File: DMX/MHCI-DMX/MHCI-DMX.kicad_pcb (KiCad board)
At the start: 2 copper layers, 79 x 90 mm, 73 parts, among them J1 XLR_Male, J10 Conn_01x02, J11 Conn_01x02, J12 Conn_01x02, J13 Conn_01x02, J14 Conn_01x02, J15 Conn_01x02, J16 Conn_01x04, J17 Conn_01x08, J18 Conn_01x04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

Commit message: v1.0 Production Files
Small ground connection fixed.
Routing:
- net GND: track 4.38 -> 6.13 mm
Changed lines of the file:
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@@
 				(font
 					(size 1.27 1.27)
+					(thickness 0.15)
 				)
 			)
@@
 				(font
 					(size 1.27 1.27)
+					(thickness 0.15)
 				)
 			)
@@
 				(font
 					(size 1.27 1.27)
+					(thickness 0.15)
 				)
 			)
@@
 				(font
 					(size 1.27 1.27)
+					(thickness 0.15)
 				)
 			)
@@
 				(font
 					(size 1.27 1.27)
+					(thickness 0.15)
 				)
 			)
@@
 				(font
 					(size 1.27 1.27)
+					(thickness 0.15)
 				)
 			)
@@
 				(font
 					(size 1.27 1.27)
+					(thickness 0.15)
 				)
 			)
@@
 				(font
 					(size 1.27 1.27)
+					(thickness 0.15)
 				)
 			)
@@
 				(font
 					(size 1.27 1.27)
+					(thickness 0.15)
 				)
 			)
@@
 				(font
 					(size 1.27 1.27)
+					(thickness 0.15)
 				)
 			)
@@
 				(font
 					(size 1.27 1.27)
+					(thickness 0.15)
 				)
 			)
@@
 				(font
 					(size 1.27 1.27)
+					(thickness 0.15)
 				)
 			)
@@
 				(font
 					(size 1.27 1.27)
+					(thickness 0.15)
 				)
 			)
@@
 				(font
 					(size 1.27 1.27)
+					(thickness 0.15)
 				)
 			)
@@
 				(font
 					(size 1.27 1.27)
+					(thickness 0.15)
 				)
 			)
@@
 				(font
 					(size 1.27 1.27)
+					(thickness 0.15)
 				)
 			)
@@
 				(font
 					(size 1.27 1.27)
+					(thickness 0.15)
 				)
 			)
@@
 				(font
 					(size 1.27 1.27)
+					(thickness 0.15)
 				)
 			)
@@
 				(font
 					(size 1.27 1.27)
+					(thickness 0.15)
 				)
 			)
@@
 				(font
 					(size 1.27 1.27)
+					(thickness 0.15)
 				)
 			)
@@
 				(font
 					(size 1.27 1.27)
+					(thickness 0.15)
 				)
 			)
@@
 				(font
 					(size 1.27 1.27)
+					(thickness 0.15)
 				)
 			)
@@
 				(font
 					(size 1.27 1.27)
+					(thickness 0.15)
 				)
 			)
@@
 				(font
 					(size 1.27 1.27)
+					(thickness 0.15)
 				)
 			)
@@
 				(font
 					(size 1.27 1.27)
+					(thickness 0.15)
 				)
 			)
@@
 				(font
 					(size 1.27 1.27)
+					(thickness 0.15)
 				)
 			)
@@
 				(font
 					(size 1.27 1.27)
+					(thickness 0.15)
 				)
 			)
@@
 				(font
 					(size 1.27 1.27)
+					(thickness 0.15)
 				)
 			)
@@
 				(font
 					(size 1.27 1.27)
+					(thickness 0.15)
 				)
 			)
@@
 				(font
 					(size 1.27 1.27)
+					(thickness 0.15)
 				)
 			)
@@
 				(font
 					(size 1.27 1.27)
+					(thickness 0.15)
 				)
 			)
@@
 				(font
 					(size 1.27 1.27)
+					(thickness 0.15)
 				)
 			)
@@
 				(font
 					(size 1.27 1.27)
+					(thickness 0.15)
 				)
 			)
@@
 				(font
 					(size 1.27 1.27)
+					(thickness 0.15)
 				)
 			)
@@
 				(font
 					(size 1.27 1.27)
+					(thickness 0.15)
 				)
 			)
@@
 				(font
 					(size 1.27 1.27)
+					(thickness 0.15)
 				)
 			)
@@
 				(font
 					(size 1.27 1.27)
+					(thickness 0.15)
 				)
 			)
@@
 				(font
 					(size 1.27 1.27)
+					(thickness 0.15)
 				)
 			)
@@
 				(font
 					(size 1.27 1.27)
+					(thickness 0.15)
 				)
 			)
@@
 	)
 	(segment
+		(start 115.895 96.125)
+		(end 115.895 95.815001)
+		(width 0.3)
+		(layer "F.Cu")
+		(net 2)
+	)
+	(segment
 		(start 76.3625 84.05)
 		(end 75.75 84.05)
@@
 		(layer "F.Cu")
 		(net 2)
+	)
+	(segment
+		(start 115.895 95.815001)
+		(end 116.710001 95)
+		(width 0.3)
+		(layer "F.Cu")
+		(net 2)
+	)
+	(segment
+		(start 116.710001 95)
+		(end 117 95)
+		(width 0.3)
+		(layer "F.Cu")
+		(net 2)

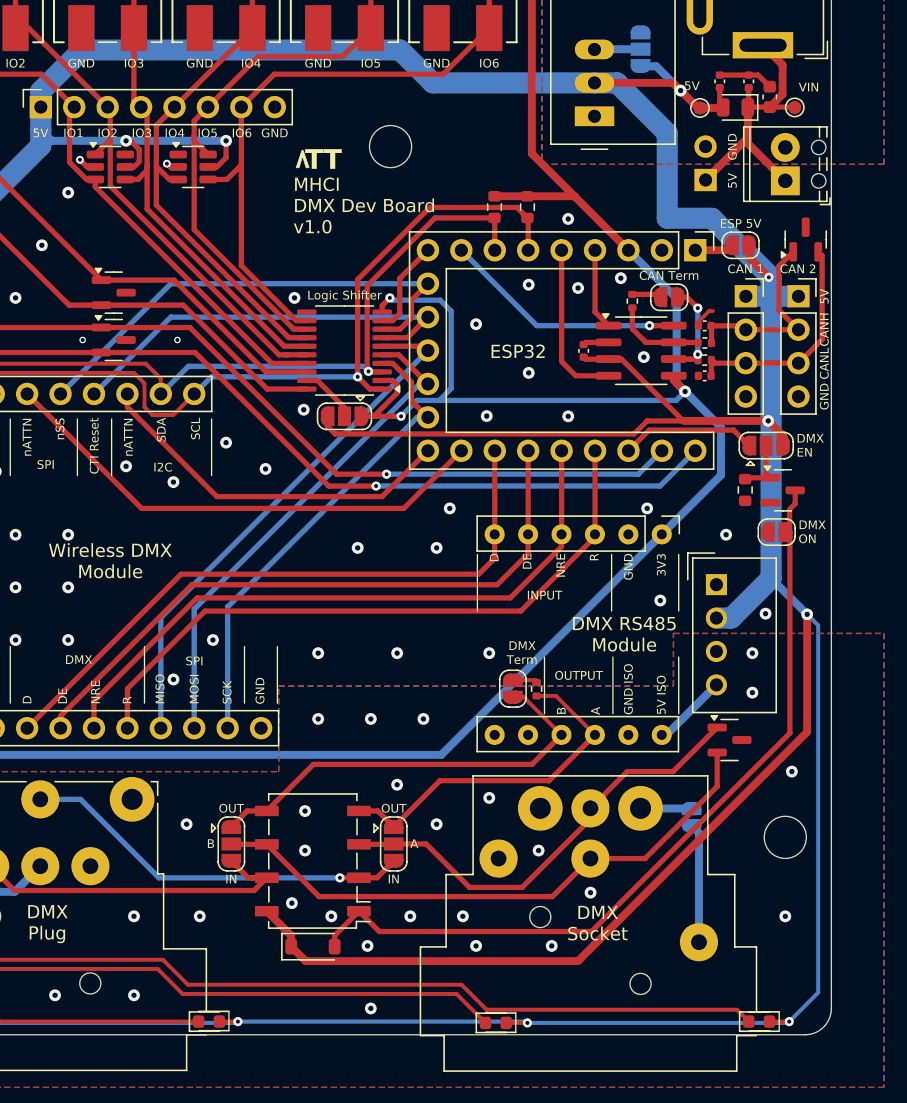
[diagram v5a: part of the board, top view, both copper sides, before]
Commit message: Update DMX board with v1.1 updates
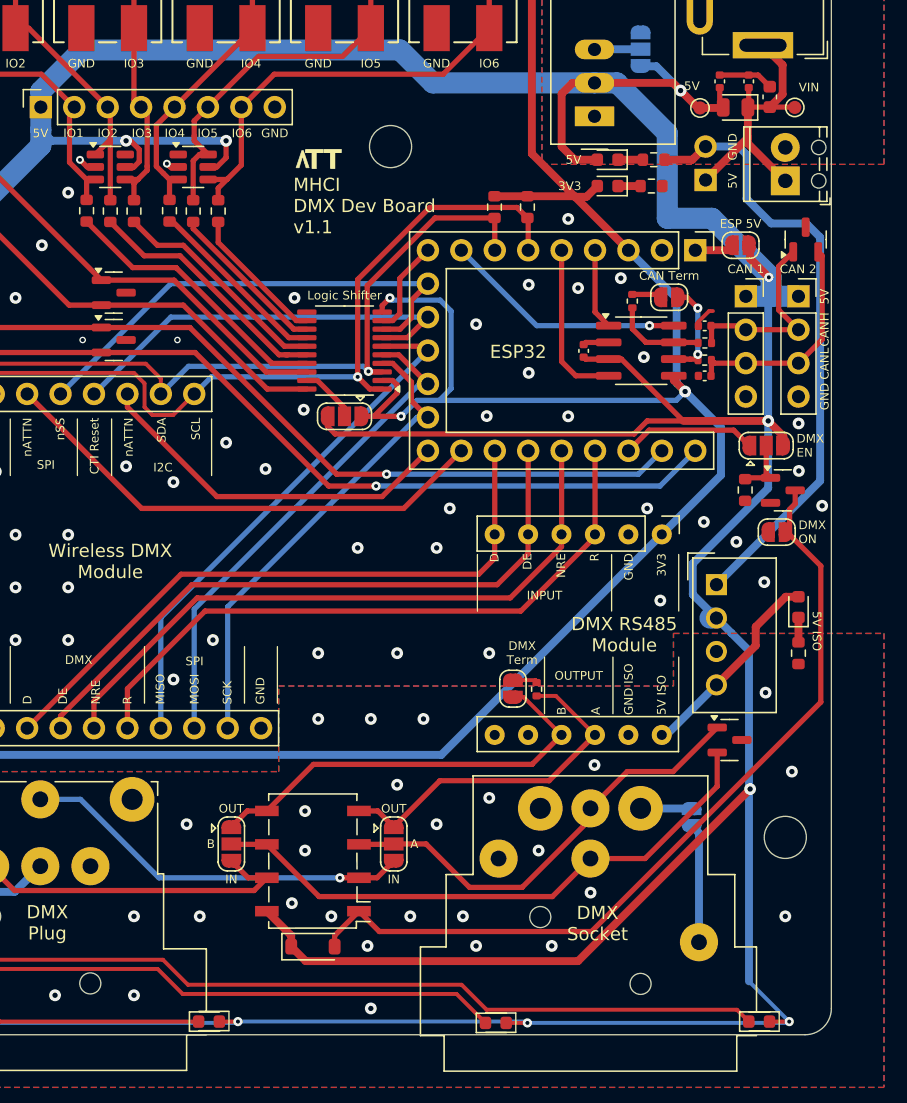
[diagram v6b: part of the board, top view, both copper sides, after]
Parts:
- added D11: RED, LED_SMD:LED_0603_1608Metric, F.Cu at (109.0, 83.5)
- added D12: RED, LED_SMD:LED_0603_1608Metric, F.Cu at (123.5, 117.5)
- added D13: RED, LED_SMD:LED_0603_1608Metric, F.Cu at (109.0, 85.5)
- added R14: 680R, Resistor_SMD:R_0603_1608Metric, F.Cu at (112.5, 83.5)
- added R15: 680R, Resistor_SMD:R_0603_1608Metric, F.Cu at (123.5, 121.0)
- added R16: 680R, Resistor_SMD:R_0603_1608Metric, F.Cu at (112.3, 85.5)
- added R17: 1K, Resistor_SMD:R_0603_1608Metric, F.Cu at (69.4, 87.4)
- added R18: 1K, Resistor_SMD:R_0603_1608Metric, F.Cu at (71.2, 87.4)
- added R19: 1K, Resistor_SMD:R_0603_1608Metric, F.Cu at (73.0, 87.4)
- added R20: 1K, Resistor_SMD:R_0603_1608Metric, F.Cu at (75.7, 87.4)
- added R21: 1K, Resistor_SMD:R_0603_1608Metric, F.Cu at (77.5, 87.4)
- added R22: 1K, Resistor_SMD:R_0603_1608Metric, F.Cu at (79.4, 87.4)
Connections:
- U5 pad 1: GND -> Earth
- U8 pad 12: GPIO_X6_5 -> Net-(U8-B8)
- U8 pad 13: GPIO_X5_5 -> Net-(U8-B7)
- U8 pad 14: GPIO_X4_5 -> Net-(U8-B6)
- U8 pad 15: GPIO_X3_5 -> Net-(U8-B5)
- U8 pad 16: GPIO_X2_5 -> Net-(U8-B4)
- U8 pad 17: GPIO_X1_5 -> Net-(U8-B3)
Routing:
- net Earth: track 4.17 -> 50.9 mm
- net Net-(U8-B3): track 0.00 -> 21.2 mm
- net GPIO_X1_5: track 54.2 -> 33.6 mm
- net GPIO_X2_5: track 46.9 -> 27.5 mm
- net Net-(U8-B4): track 0.00 -> 19.3 mm
- net GPIO_X3_5: track 41.8 -> 23.8 mm
- net Net-(U8-B5): track 0.00 -> 17.1 mm
- net GPIO_X4_5: track 43.4 -> 26.4 mm
- net GPIO_X5_5: track 47.4 -> 32.9 mm
- net Net-(U8-B6): track 0.00 -> 14.1 mm
- net GPIO_X6_5: track 52.3 -> 39.8 mm
- net Net-(U8-B7): track 0.00 -> 12.3 mm
- net Net-(U8-B8): track 0.00 -> 10.8 mm
- net +5V_ISO: track 5.73 -> 16.0 mm
- net +5V: track 371.5 -> 364.6 mm
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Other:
- board text added: "MHCI DMX Dev Board v1.1"
- board text removed: "MHCI DMX Dev Board v1.0"

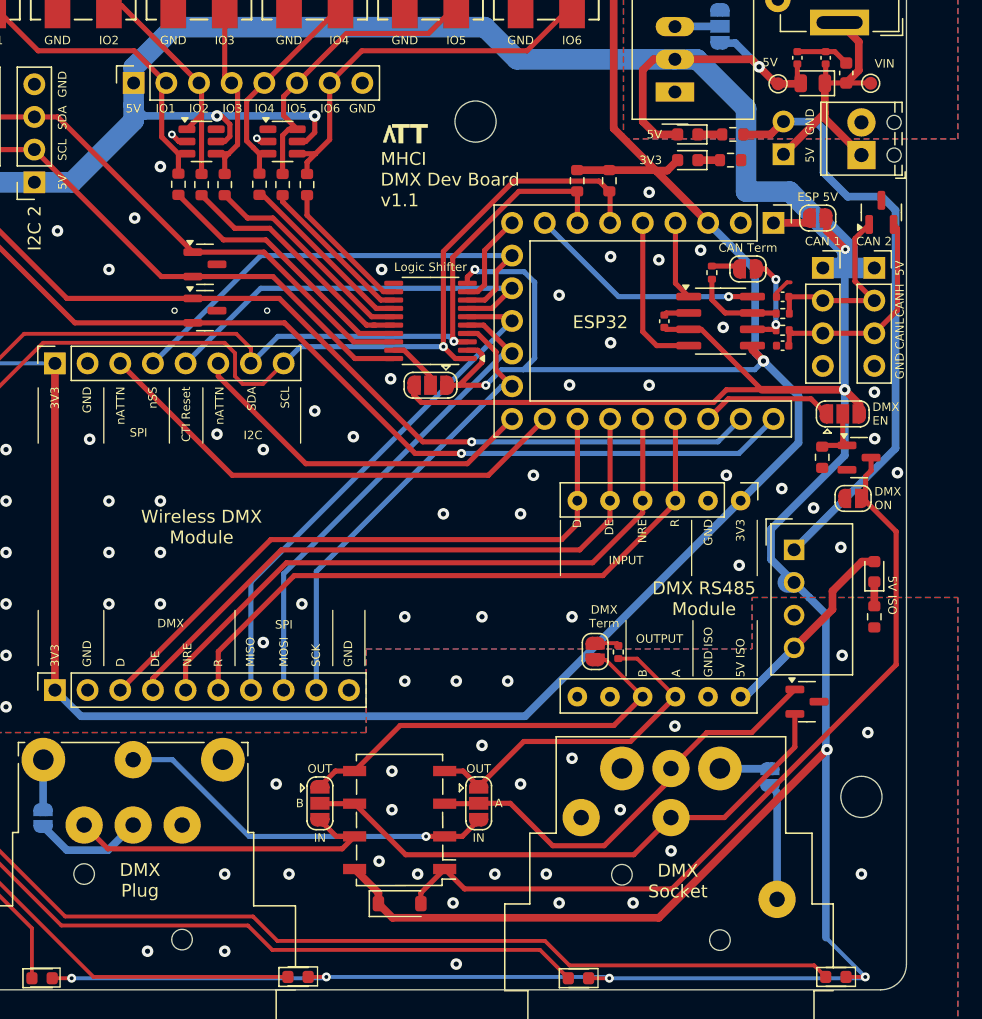
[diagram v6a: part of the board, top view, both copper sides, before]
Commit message: MHCI-DMX v1.1 hardware
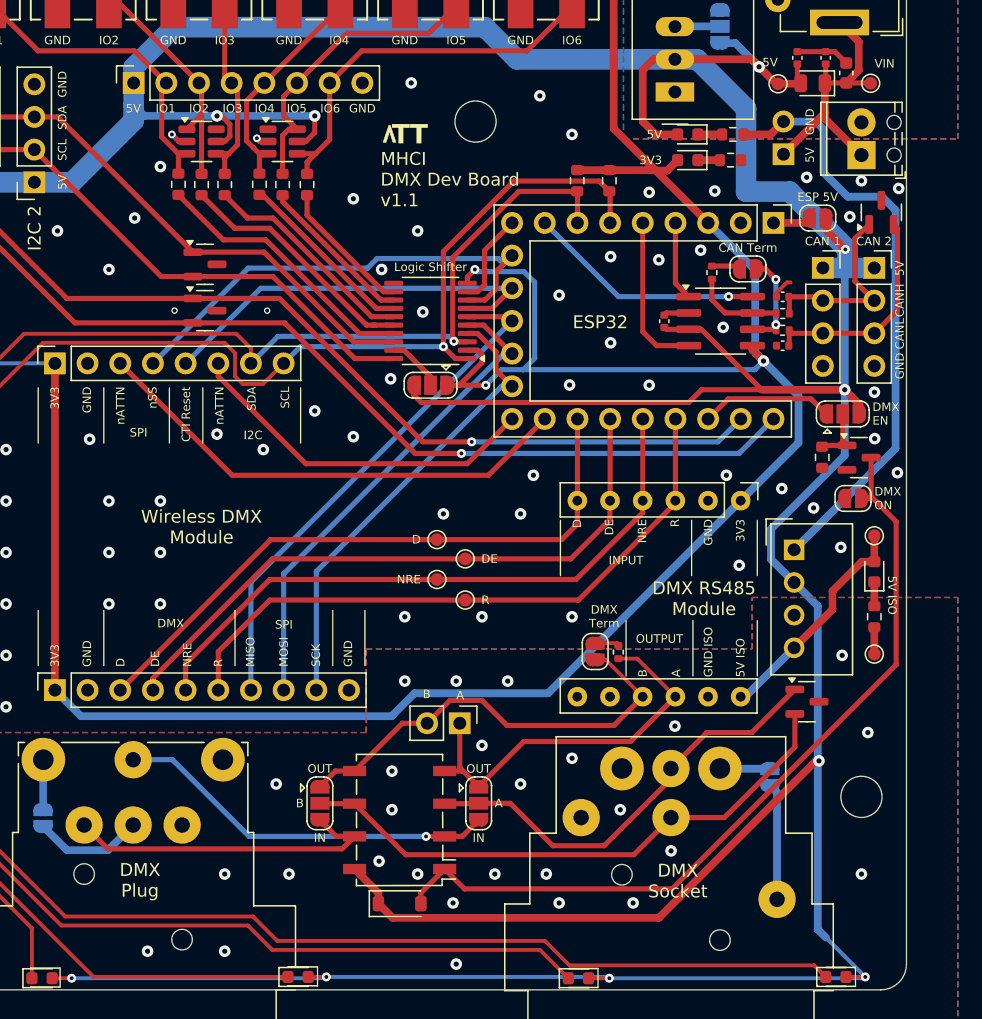
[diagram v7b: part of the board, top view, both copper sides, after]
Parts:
- added J19: Conn_01x02, Connector_PinHeader_2.54mm:PinHeader_1x02_P2.54mm_Vertical, F.Cu at (91.3, 129.3)
- added TP3: 5V_ISO, TestPoint:TestPoint_Pad_D1.0mm, F.Cu at (123.5, 114.7)
- added TP4: GND_DMX, TestPoint:TestPoint_Pad_D1.0mm, F.Cu at (123.5, 123.9)
- added TP5: D, TestPoint:TestPoint_Pad_D1.0mm, F.Cu at (89.5, 115.0)
- added TP6: DE, TestPoint:TestPoint_Pad_D1.0mm, F.Cu at (91.7, 116.5)
- added TP7: NRE, TestPoint:TestPoint_Pad_D1.0mm, F.Cu at (89.5, 118.1)
- added TP8: R, TestPoint:TestPoint_Pad_D1.0mm, F.Cu at (91.7, 119.7)
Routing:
- net A: track 26.9 -> 30.7 mm
- net GND_DMX: track 7.78 -> 9.86 mm
- net +5V_ISO: track 16.0 -> 18.1 mm
- net B: track 32.9 -> 34.5 mm
- net +5V: track 364.6 -> 363.1 mm
- net GND: vias 68 -> 77

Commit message: MHCI DMX v1.2 production files
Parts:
- removed J9: Conn_01x02, Connector_PinHeader_2.54mm:PinHeader_1x02_P2.54mm_Vertical
- removed TP1: VIN, TestPoint:TestPoint_Pad_D1.0mm
- removed TP2: 5V, TestPoint:TestPoint_Pad_D1.0mm
- added J3: Conn_01x02, Connector_PinHeader_2.54mm:PinHeader_1x02_P2.54mm_Vertical, F.Cu at (112.7, 73.1)
- added U6: TSR_2-2450, Converter_DCDC:Converter_DCDC_TRACO_TSR-1_THT, F.Cu at (108.5, 72.4)
- J5: value Conn_01x02 -> Conn_01x04; footprint TerminalBlock_Phoenix:TerminalBlock_Phoenix_MPT-0,5-2-2.54_1x02_P2.54mm_Horizontal -> Connector_PinHeader_2.54mm:PinHeader_1x04_P2.54mm_Vertical
- moved J5 28.7 mm to (105.8, 61.8)
- moved C4 16.2 mm to (113.9, 64.3), turned to 180 degrees
- moved U4 15.7 mm to (123.6, 82.4), turned to 180 degrees
- moved R16 14.6 mm to (98.8, 80.0), turned to 90 degrees
- moved C5 13.6 mm to (112.7, 65.9), turned to 0 degrees
- moved FB1 13.2 mm to (114.7, 66.9), turned to -90 degrees
- moved R14 11.8 mm to (100.7, 83.6), turned to -90 degrees
- moved C6 10.6 mm to (112.7, 68.1), turned to 180 degrees
- moved D13 10.4 mm to (98.8, 83.5), turned to -90 degrees
- moved JP14 10.4 mm to (121.1, 79.0), turned to 180 degrees
- moved D11 8.97 mm to (100.7, 80.1), turned to 90 degrees
- moved J6 0.63 mm to (120.8, 74.2)
- moved R5 0.54 mm to (102.4, 87.1)
- moved D5 0.43 mm to (124.0, 90.0)
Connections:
- C4 pad 1: VIN -> +5V
- C4 pad 2: Earth -> GND
- C5 pad 1: Earth -> GND
- C5 pad 2: VIN -> +5V
- C6 pad 1: +5V -> /5V filtered
- C6 pad 2: Earth -> GND
- FB1 pad 1: VIN -> +5V
- FB1 pad 2: +5V -> /5V filtered
- J5 pad 1: VIN -> VCC
- J5 pad 2: Earth -> GND
- J6 pad 1: VIN -> +5V
- J6 pad 2: Earth -> GND
- JP14 pad 1: Earth -> GND
- JP14 pad 3: +5V -> /5V filtered
- R14 pad 2: Earth -> GND
- U4 pad 1: Earth -> GND
- U4 pad 2: +5V -> /5V filtered
- U5 pad 1: Earth -> GND
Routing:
- net Earth: track 50.9 -> 0.00 mm
- net VIN: track 22.1 -> 0.00 mm
- net /5V filtered: track 0.00 -> 20.8 mm, vias 0 -> 1
- net VCC: track 0.00 -> 12.0 mm
- net +5V: track 363.1 -> 374.1 mm, vias 10 -> 11
- net GND: track 6.13 -> 10.3 mm, vias 77 -> 80
- net +3V3: track 213.3 -> 209.9 mm
- net Net-(JP14-C): track 3.51 -> 4.47 mm
- removed copper zone on B.Cu, net Earth
- removed copper zone on F.Cu, net Earth
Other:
- board text added: "EN"
- board text added: "ISO"
- board text added: "MHCI DMX Dev Board v1.2"
- board text removed: "MHCI DMX Dev Board v1.1"
